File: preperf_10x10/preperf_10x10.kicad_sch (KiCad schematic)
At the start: 1 part, among them J1 Conn_01x02_Pin

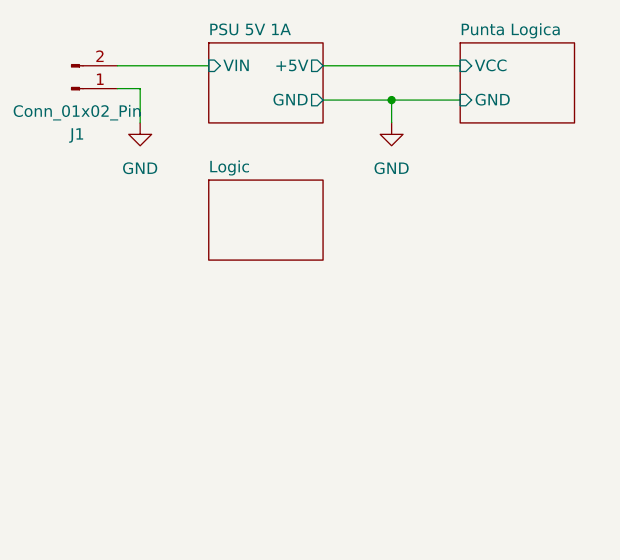
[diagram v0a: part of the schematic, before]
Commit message: Added TP2, TP3 and TP4
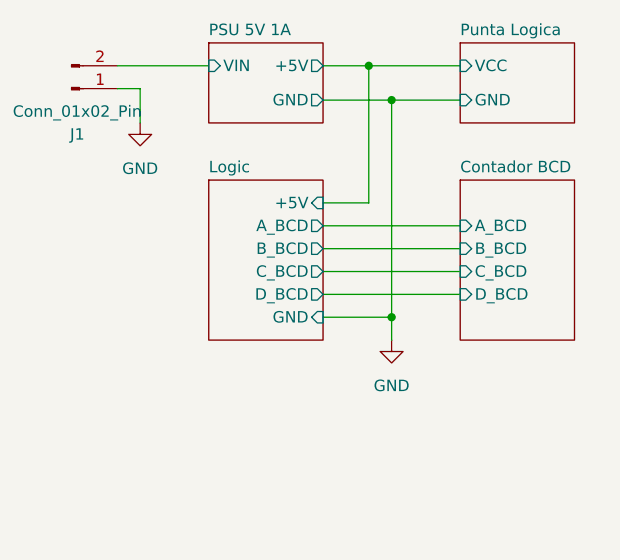
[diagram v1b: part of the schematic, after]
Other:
- added sheet Contador BCD (bcd_counter.kicad_sch)
- sheet Logic ports: added +5V, A_BCD, B_BCD, C_BCD, D_BCD, GND; removed none
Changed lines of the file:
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@@
 (kicad_sch (version 20230121) (generator eeschema)
   (paper "A4")
+  (junction (at 153.67 57.15) (diameter 0) (color 0 0 0 0)
+  )
+  (junction (at 151.13 29.21) (diameter 0) (color 0 0 0 0)
+  )
   (junction (at 153.67 33.02) (diameter 0) (color 0 0 0 0)
   )
-  (wire (pts (xy 146.05 29.21) (xy 161.29 29.21))
+  (wire (pts (xy 146.05 29.21) (xy 151.13 29.21))
     (stroke (width 0) (type default))
   )
@@
     (stroke (width 0) (type default))
   )
-  (wire (pts (xy 153.67 33.02) (xy 153.67 35.56))
+  (wire (pts (xy 146.05 44.45) (xy 151.13 44.45))
+    (stroke (width 0) (type default))
+  )
+  (wire (pts (xy 153.67 57.15) (xy 153.67 59.69))
+    (stroke (width 0) (type default))
+  )
+  (wire (pts (xy 146.05 49.53) (xy 161.29 49.53))
+    (stroke (width 0) (type default))
+  )
+  (wire (pts (xy 151.13 29.21) (xy 151.13 44.45))
     (stroke (width 0) (type default))
   )
@@
     (stroke (width 0) (type default))
   )
+  (wire (pts (xy 146.05 46.99) (xy 161.29 46.99))
+    (stroke (width 0) (type default))
+  )
+  (wire (pts (xy 146.05 57.15) (xy 153.67 57.15))
+    (stroke (width 0) (type default))
+  )
+  (wire (pts (xy 153.67 33.02) (xy 153.67 57.15))
+    (stroke (width 0) (type default))
+  )
+  (wire (pts (xy 146.05 54.61) (xy 161.29 54.61))
+    (stroke (width 0) (type default))
+  )
   (wire (pts (xy 146.05 33.02) (xy 153.67 33.02))
+    (stroke (width 0) (type default))
+  )
+  (wire (pts (xy 146.05 52.07) (xy 161.29 52.07))
+    (stroke (width 0) (type default))
+  )
+  (wire (pts (xy 151.13 29.21) (xy 161.29 29.21))
     (stroke (width 0) (type default))
   )
@@
     )
   )
-  (symbol (lib_id "power:GND") (at 153.67 35.56 0) (unit 1)
+  (symbol (lib_id "power:GND") (at 153.67 59.69 0) (unit 1)
     (in_bom yes) (on_board yes) (dnp no) (fields_autoplaced)
-    (property "Reference" "#PWR02" (at 153.67 41.91 0)
-      (effects (font (size 1.27 1.27)) hide)
-    )
-    (property "Value" "GND" (at 153.67 40.64 0)
+    (property "Reference" "#PWR02" (at 153.67 66.04 0)
+      (effects (font (size 1.27 1.27)) hide)
+    )
+    (property "Value" "GND" (at 153.67 64.77 0)
       (effects (font (size 1.27 1.27)))
     )
-    (property "Footprint" "" (at 153.67 35.56 0)
-      (effects (font (size 1.27 1.27)) hide)
-    )
-    (property "Datasheet" "" (at 153.67 35.56 0)
+    (property "Footprint" "" (at 153.67 59.69 0)
+      (effects (font (size 1.27 1.27)) hide)
+    )
+    (property "Datasheet" "" (at 153.67 59.69 0)
       (effects (font (size 1.27 1.27)) hide)
     )
@@
     )
   )
-  (sheet (at 133.35 41.91) (size 12.7 8.89) (fields_autoplaced)
+  (sheet (at 133.35 41.91) (size 12.7 17.78) (fields_autoplaced)
     (stroke (width 0.1524) (type solid))
     (fill (color 0 0 0 0.0000))
@@
       (effects (font (size 1.27 1.27)) (justify left bottom))
     )
-    (property "Sheetfile" "logic_gates.kicad_sch" (at 133.35 51.3846 0)
+    (property "Sheetfile" "logic_gates.kicad_sch" (at 133.35 60.2746 0)
       (effects (font (size 1.27 1.27)) (justify left top) hide)
+    )
+    (pin "+5V" input (at 146.05 44.45 0)
+      (effects (font (size 1.27 1.27)) (justify right))
+    )
+    (pin "GND" input (at 146.05 57.15 0)
+      (effects (font (size 1.27 1.27)) (justify right))
+    )
+    (pin "C_BCD" output (at 146.05 52.07 0)
+      (effects (font (size 1.27 1.27)) (justify right))
+    )
+    (pin "D_BCD" output (at 146.05 54.61 0)
+      (effects (font (size 1.27 1.27)) (justify right))
+    )
+    (pin "B_BCD" output (at 146.05 49.53 0)
+      (effects (font (size 1.27 1.27)) (justify right))
+    )
+    (pin "A_BCD" output (at 146.05 46.99 0)
+      (effects (font (size 1.27 1.27)) (justify right))
     )
     (instances
@@
       )
     )
+  )
+  (sheet (at 161.29 41.91) (size 12.7 17.78) (fields_autoplaced)
+    (stroke (width 0.1524) (type solid))
+    (fill (color 0 0 0 0.0000))
+    (property "Sheetname" "Contador BCD" (at 161.29 41.1984 0)
+      (effects (font (size 1.27 1.27)) (justify left bottom))
+    )
+    (property "Sheetfile" "bcd_counter.kicad_sch" (at 161.29 60.2746 0)
+      (effects (font (size 1.27 1.27)) (justify left top) hide)
+    )
+    (pin "A_BCD" input (at 161.29 46.99 180)
+      (effects (font (size 1.27 1.27)) (justify left))
+    )
+    (pin "B_BCD" input (at 161.29 49.53 180)
+      (effects (font (size 1.27 1.27)) (justify left))
+    )
+    (pin "C_BCD" input (at 161.29 52.07 180)
+      (effects (font (size 1.27 1.27)) (justify left))
+    )
+    (pin "D_BCD" input (at 161.29 54.61 180)
+      (effects (font (size 1.27 1.27)) (justify left))
+    )
+    (instances
+      (project "preperf_10x10"
+        (path "/7bf6ff06-236f-433e-86e9-cc0b656b998f" (page "5"))
+      )
+    )

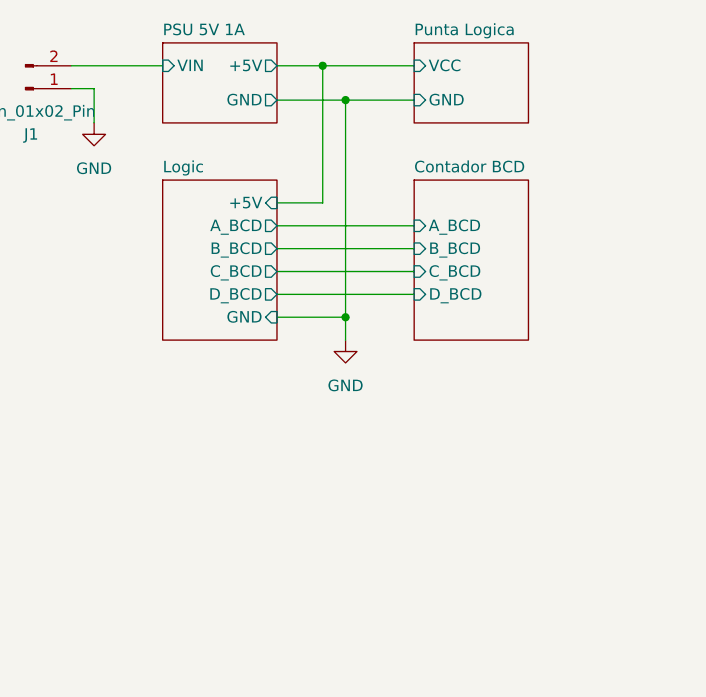
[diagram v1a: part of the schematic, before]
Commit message: "TP2" and "TP3" digital techniques
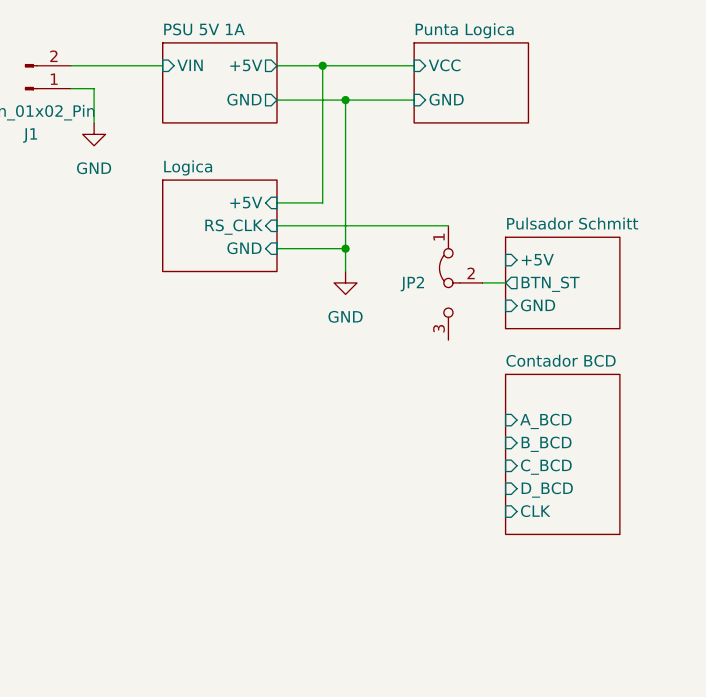
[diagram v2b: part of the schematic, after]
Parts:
- added JP2: Jumper_3_Bridged12, Connector_PinHeader_2.54mm:PinHeader_1x03_P2.54mm_Vertical, symbol Jumper:Jumper_3_Bridged12
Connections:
- new net Logica/RS_CLK: JP2.1 (A)
- new net Pulsador Schmitt/BTN_ST: JP2.2 (C)
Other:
- sheet Logic renamed Logica
- added sheet Pulsador Schmitt (schmittTrigger.kicad_sch)
- sheet Contador BCD ports: added CLK; removed none
- sheet Logica ports: added RS_CLK; removed A_BCD, B_BCD, C_BCD, D_BCD

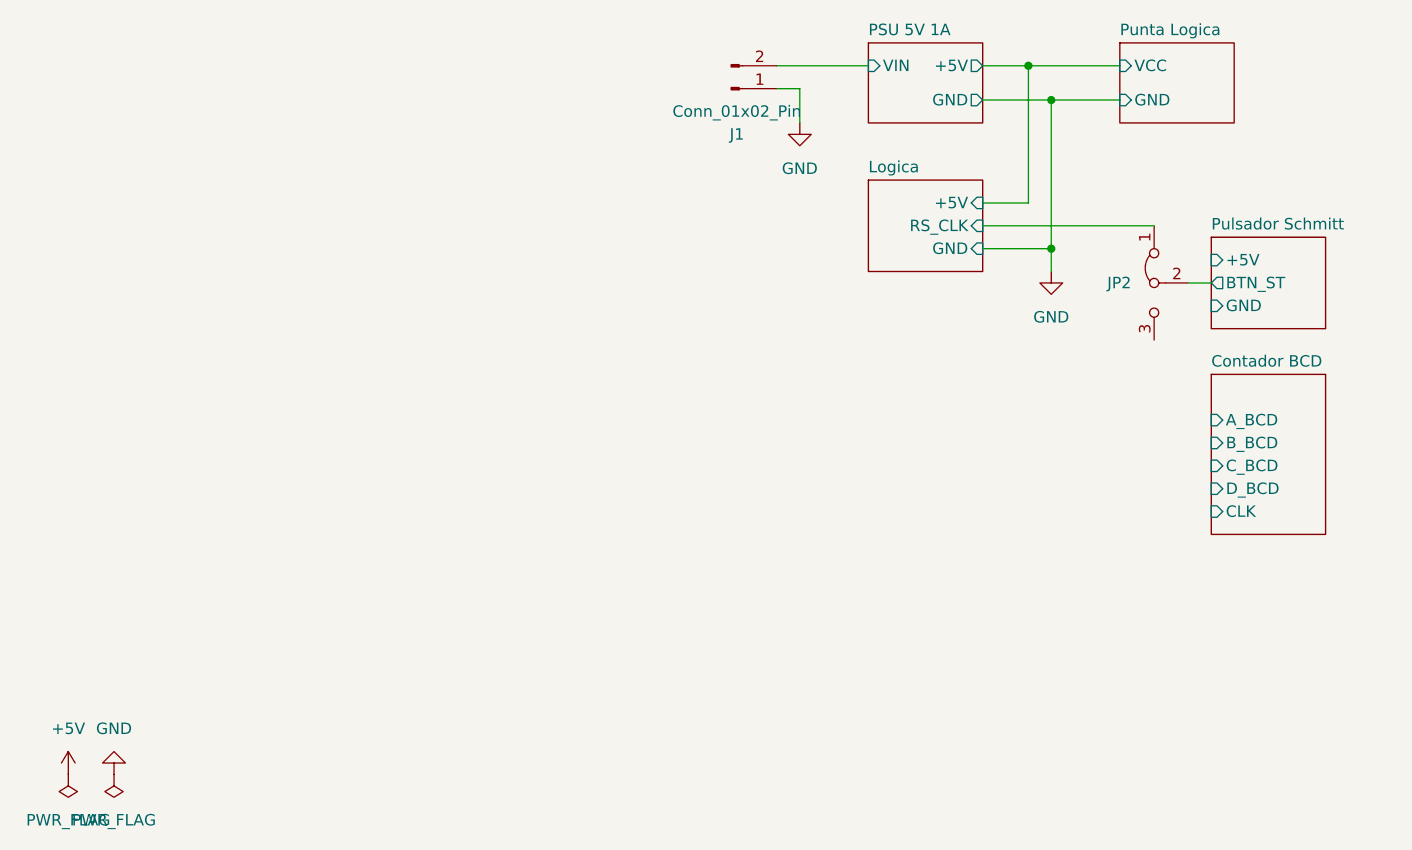
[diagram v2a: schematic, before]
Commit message: Added BCD Up counter with JK FF
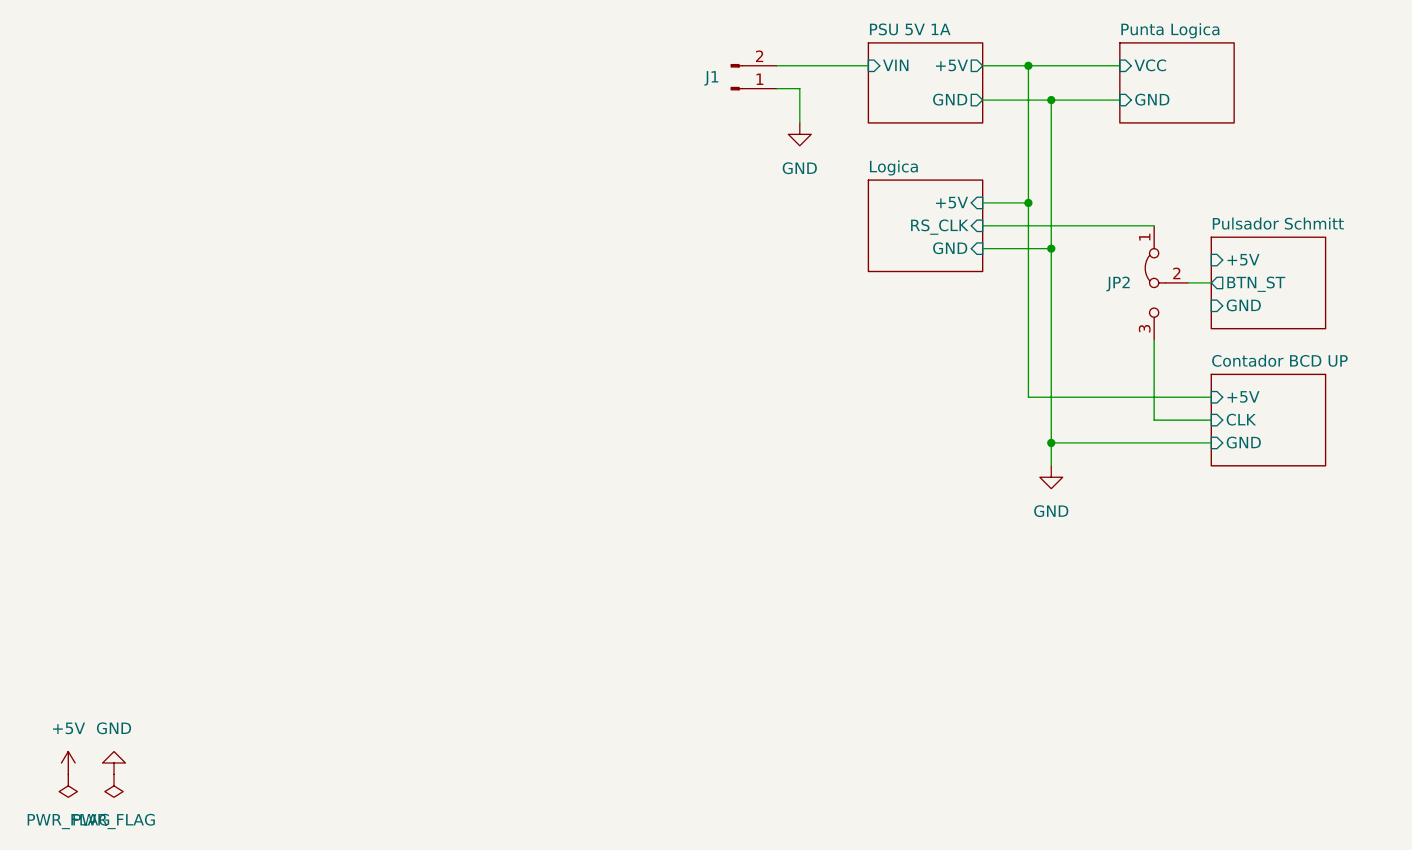
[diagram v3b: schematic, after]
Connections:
- net Contador BCD UP/CLK: now also JP2.3 (B)
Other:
- sheet Contador BCD renamed Contador BCD UP
- sheet Contador BCD UP ports: added +5V, GND; removed A_BCD, B_BCD, C_BCD, D_BCD

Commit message: [ADD] Digital Logic Design project (FIUBA): PCB implementation of schmitt triggers, logic functions, counters, state machines, and logic probes
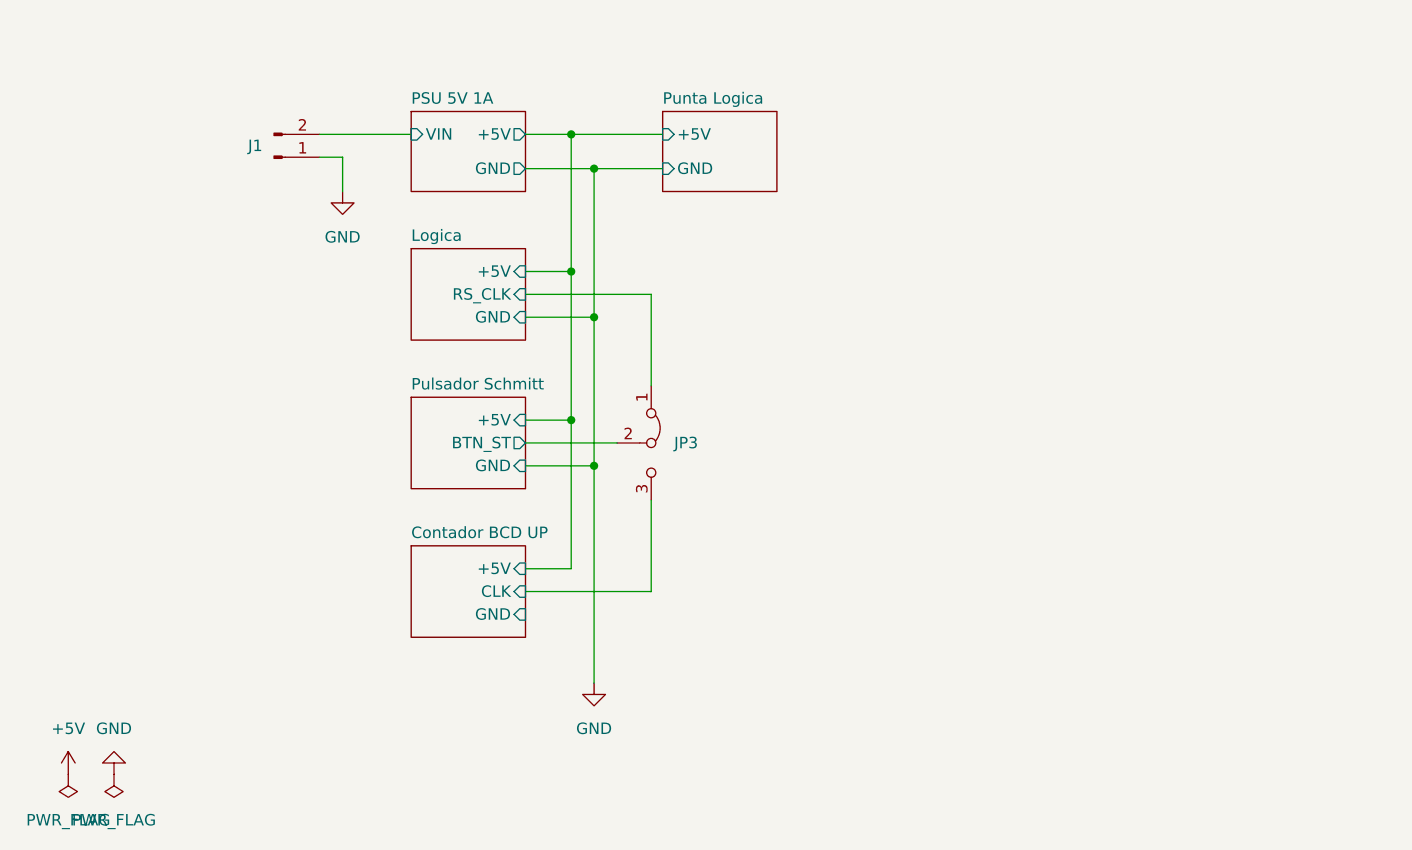
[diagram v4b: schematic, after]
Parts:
- renumbered JP2 to JP3
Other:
- sheet Punta Logica ports: added +5V; removed VCC
- moved on the sheet: J1, JP3
